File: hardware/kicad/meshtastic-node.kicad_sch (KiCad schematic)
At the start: 18 parts, among them Q1 AO3401A, SW1 rocker ON/OFF, SW2 user button, U1 ESP32-S3-DevKitC-1, U2 E22-400M22S (SX1268), U3 GY-NEO8MV2, U4 SSD1306 128x64, U5 TP4056, U6 TPS63020

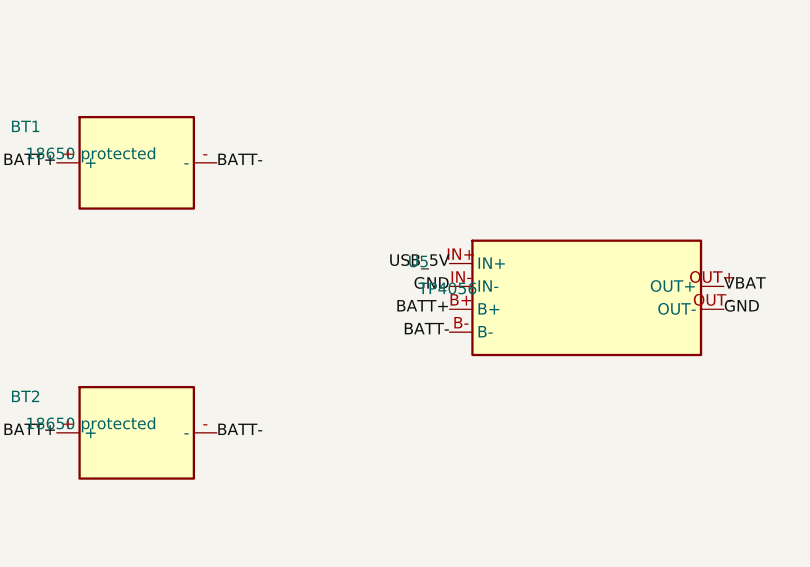
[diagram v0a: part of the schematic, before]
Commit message: Fix TP4056 ground short, build idempotency, and doc issues from code review
- Split U5.IN- onto a dedicated USB_GND net instead of GND, so the
  netlist/KiCad schematic no longer bridges the TP4056's low-side
  protection MOSFETs (netlist.txt, gen_kicad.py, kicad_sch)
- gen_kicad.py: deterministic uuid5 symbol/pin UUIDs and pathlib-anchored
  output paths, so re-running produces no diff and always writes
  hardware/netlist.txt regardless of cwd
- Makefile: firmware-install now copies platformio-env.ini into
  variants/<env>/platformio.ini (picked up via PlatformIO's extra_configs)
  instead of a grep-guarded append, so edits always take effect; harness
  target now outputs directly to docs/ to match README/docs references
- variant.h: add #pragma once
- docs: note GPIO5 GPS-UART backfeed mitigation and USB-contention
  hardening option in build.md, TP4056 charge time in bom.md, and fix
  the GPS VCC wire color in power-schematic.svg/png to match other rails

Co-Authored-By: Claude Sonnet 5 <noreply@anthropic.com>
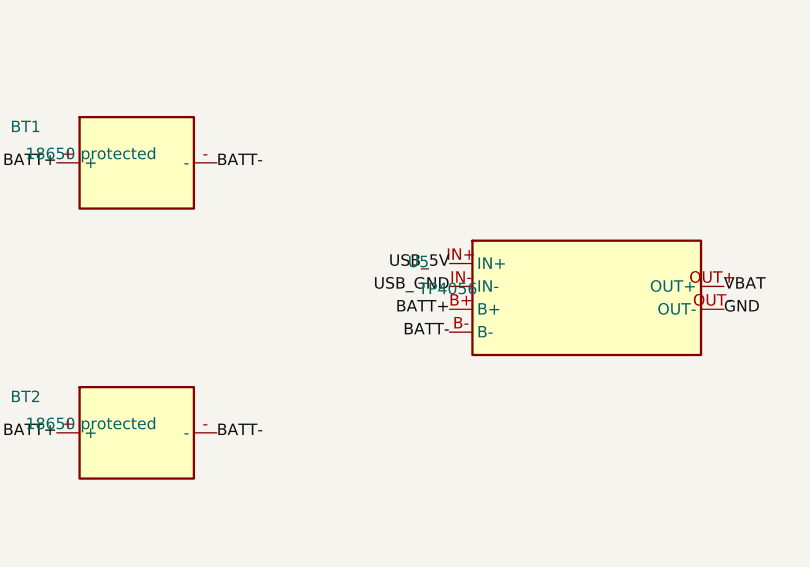
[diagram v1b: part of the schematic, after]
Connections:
- net GND: no longer U5.IN-
- new net USB_GND: U5.IN-
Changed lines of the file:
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@@
     (effects (font (size 1.27 1.27)) (justify left))
-  )
-  (label "GND" (at 74.76 218.73 0)
-    (effects (font (size 1.27 1.27)) (justify right))
   )
   (label "GND" (at 132.22 266.27 0)
@@
   )
   (label "USB_5V" (at 74.76 216.19 0)
+    (effects (font (size 1.27 1.27)) (justify right))
+  )
+  (label "USB_GND" (at 74.76 218.73 0)
     (effects (font (size 1.27 1.27)) (justify right))
   )
@@
   )
   (symbol_instances
-    (path "/c709f035-7dde-4bfb-9a0a-a2c2d14464c8"
+    (path "/df90c69f-ad25-5db9-9646-89e96fc1902d"
       (reference "U1") (unit 1) (value "ESP32-S3-DevKitC-1") (footprint "")
     )
-    (path "/d475e183-04fd-4d10-837c-3d54e80d5a4d"
+    (path "/cf4e88f5-a5ad-5934-8b39-1279e742636b"
       (reference "U2") (unit 1) (value "E22-400M22S (SX1268)") (footprint "")
     )
-    (path "/57d6e93b-f92d-4903-b625-d8d779e80037"
+    (path "/76849281-e581-5f9b-b5d9-263073e3398e"
       (reference "U3") (unit 1) (value "GY-NEO8MV2") (footprint "")
     )
-    (path "/cced5920-86af-41a3-9869-0f71a6b8a098"
+    (path "/d402735e-ecbd-5600-860c-5ba78f8ffb3f"
       (reference "U4") (unit 1) (value "SSD1306 128x64") (footprint "")
     )
-    (path "/2484cda1-9ba2-44f1-bd37-93abc4b7908d"
+    (path "/b0fc57a0-b847-50c8-a585-ea4969ceae41"
       (reference "U5") (unit 1) (value "TP4056") (footprint "")
     )
-    (path "/4d82a1e3-5c05-452c-b2a1-5e35ad64da7d"
+    (path "/7ed61422-9f5e-50ea-acbc-86d590d20f83"
       (reference "U6") (unit 1) (value "TPS63020") (footprint "")
     )
-    (path "/8e8c1d12-9d7e-44cf-86b8-4542ca0408a3"
+    (path "/c85a521f-a8ab-521e-889c-85029ad1b39a"
       (reference "Q1") (unit 1) (value "AO3401A") (footprint "")
     )
-    (path "/f27627bf-67d1-4d43-94d1-16e5aff71d51"
+    (path "/31df9366-a700-54b6-90e4-cc4f85b61a8a"
       (reference "R1") (unit 1) (value "100k 1%") (footprint "")
     )
-    (path "/655d7195-0834-40fb-81d1-e11abde1153c"
+    (path "/8dba7662-a31d-5c89-bd57-3d3c92440d3d"
       (reference "R2") (unit 1) (value "100k 1%") (footprint "")
     )
-    (path "/891c2111-4854-4eb4-825c-7f4da77f8e20"
+    (path "/4d127a15-68b8-5462-8257-bd2757737392"
       (reference "R3") (unit 1) (value "100k") (footprint "")
     )
-    (path "/fc86f714-9203-4987-b46e-95e6bd56bf97"
+    (path "/cff63d59-eafd-5ecb-92ee-e61315f0f1a9"
       (reference "C1") (unit 1) (value "470u 10V low-ESR") (footprint "")
     )
-    (path "/da548dce-149c-4981-819f-38b2d27070b8"
+    (path "/09d386b1-48ab-5b74-b62e-f5e8053c0bf3"
       (reference "C2") (unit 1) (value "10u 25V X7R") (footprint "")
     )
-    (path "/628cc0f2-6fd7-4fd5-86b6-ea05beb98ebc"
+    (path "/b955f17b-ad4b-5ef0-ab1e-2fe0c325368f"
       (reference "C3") (unit 1) (value "100n 50V X7R") (footprint "")
     )
-    (path "/60b27d8a-8adb-46dc-9779-b36bb1018e90"
+    (path "/d59bc435-7620-5550-84a3-7b79ed4a626f"
       (reference "C4") (unit 1) (value "100n 50V X7R") (footprint "")
     )
-    (path "/7135a9ce-7596-4b1e-bc9b-9203b17fb399"
+    (path "/8c97d37e-c8e5-5861-949d-45306792dba1"
       (reference "SW1") (unit 1) (value "rocker ON/OFF") (footprint "")
     )
-    (path "/48c7565f-e58f-4e02-9580-8ae01a7ebf74"
+    (path "/8a469bf1-6c44-59e9-9497-0a7b61734cdf"
       (reference "SW2") (unit 1) (value "user button") (footprint "")
     )
-    (path "/d5b532bc-a2f4-4bf3-92d6-1ca536217fc0"
+    (path "/994d9118-6c24-5b52-96ad-d5c1eba40278"
       (reference "BT1") (unit 1) (value "18650 protected") (footprint "")
     )
-    (path "/2c684270-915b-4069-bf4b-57f017c47b68"
+    (path "/5daf1e1b-6009-5805-a361-481670013e7b"
       (reference "BT2") (unit 1) (value "18650 protected") (footprint "")
     )
